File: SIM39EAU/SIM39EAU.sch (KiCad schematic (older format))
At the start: 15 parts, among them IC1 SIM39EA, J1 Conn_01x08, U2 AP7365-W-7

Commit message: Part Numbers Added
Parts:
- BT1: Part (none) -> C238097
- C3: Part (none) -> C396719
- C4: value 1uF -> 4.7uF; Part (none) -> C87998
- D1, D2: Part (none) -> C303800
- R3: Part (none) -> C99198
- R7: Part (none) -> C163436
- R8: Part (none) -> C103426
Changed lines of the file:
@@
 F 2 "Resistor_SMD:R_0603_1608Metric" V 3040 1240 50  0001 C CNN
 F 3 "~" H 3000 1250 50  0001 C CNN
+F 4 "C163436" V 3000 1250 50  0001 C CNN "Part"
 	1    3000 1250
 	0    -1   -1   0
@@
 F 2 "Resistor_SMD:R_0603_1608Metric" V 3240 1540 50  0001 C CNN
 F 3 "~" H 3200 1550 50  0001 C CNN
+F 4 "C103426" H 3200 1550 50  0001 C CNN "Part"
 	1    3200 1550
 	-1   0    0    1
@@
 F 2 "Capacitor_SMD:C_0805_2012Metric" H 1588 1400 50  0001 C CNN
 F 3 "~" H 1550 1550 50  0001 C CNN
+F 4 "C396719" H 1550 1550 50  0001 C CNN "Part"
 	1    1550 1550
 	1    0    0    -1
@@
 F 2 "Resistor_SMD:R_0603_1608Metric" V 1890 1340 50  0001 C CNN
 F 3 "~" H 1850 1350 50  0001 C CNN
+F 4 "C99198" V 1850 1350 50  0001 C CNN "Part"
 	1    1850 1350
 	0    -1   1    0
@@
 P 3450 1550
 F 0 "C4" H 3565 1595 50  0000 L CNN
-F 1 "1uF" H 3565 1505 50  0000 L CNN
+F 1 "4.7uF" H 3565 1505 50  0000 L CNN
 F 2 "Capacitor_SMD:C_0805_2012Metric" H 3488 1400 50  0001 C CNN
 F 3 "~" H 3450 1550 50  0001 C CNN
+F 4 "C87998" H 3450 1550 50  0001 C CNN "Part"
 	1    3450 1550
 	1    0    0    -1
@@
 F 2 "Battery:BatteryHolder_Keystone_3000_1x12mm" V 2700 3410 50  0001 C CNN
 F 3 "~" V 2700 3410 50  0001 C CNN
+F 4 "C238097" H 2700 3350 50  0001 C CNN "Part"
 	1    2700 3350
 	-1   0    0    -1
@@
 F 2 "Diode_SMD:D_SOD-323" H 5100 3100 50  0001 C CNN
 F 3 "https://www.vishay.com/docs/88301/15ke.pdf" H 5050 3300 50  0001 C CNN
+F 4 "C303800" H 5100 3300 50  0001 C CNN "Part"
 	1    5100 3300
 	0    1    1    0
@@
 F 2 "Diode_SMD:D_SOD-323" H 5450 3100 50  0001 C CNN
 F 3 "https://www.vishay.com/docs/88301/15ke.pdf" H 5400 3300 50  0001 C CNN
+F 4 "C303800" H 5450 3300 50  0001 C CNN "Part"
 	1    5450 3300
 	0    1    1    0

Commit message: LED Update
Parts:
- removed R7: 68K, Resistor_SMD:R_0603_1608Metric, symbol Device:R_US
- removed R8: 22K, Resistor_SMD:R_0603_1608Metric, symbol Device:R_US
- removed U2: AP7365-W-7, Package_TO_SOT_SMD:SOT-23-5, symbol Regulator_Linear:AP2127K-ADJ
- added D3: LED, LED_SMD:LED_0603_1608Metric, symbol Device:LED
- added JP1: SolderJumper_2_Bridged, Jumper:SolderJumper-2_P1.3mm_Bridged_RoundedPad1.0x1.5mm, symbol Jumper:SolderJumper_2_Bridged
- added R1: 680E, Resistor_SMD:R_0603_1608Metric, symbol Device:R_US
- added U1: AP2127K-3.3, Package_TO_SOT_SMD:SOT-23-5, symbol Regulator_Linear:AP2127K-3.3
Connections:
- net 3V3: now also JP1.1 (A), U1.5 (VOUT)
- net EN: now also U1.3 (EN)
- net GND: now also D3.1 (K), U1.2 (GND)
- net VIN: now also U1.1 (VIN)
- new net: JP1.2 (B), R1.2
- new net: D3.2 (A), R1.1
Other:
- moved on the sheet: C3, C4
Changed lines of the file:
@@
 Comment4 ""
 $EndDescr
-Text GLabel 3600 1100 2    50   Input ~ 0
+Text GLabel 3550 1250 2    50   Input ~ 0
 3V3
 Wire Wire Line
-	1550 1400 1550 1350
-Wire Wire Line
-	1550 1700 1550 1850
+	1550 1650 1550 1350
+Wire Wire Line
+	1550 1950 1550 2200
 $Comp
 L power:GND #PWR0103
 U 1 1 5DFA7870
-P 2450 1950
-F 0 "#PWR0103" H 2450 1700 50  0001 C CNN
-F 1 "GND" H 2455 1777 50  0000 C CNN
-F 2 "" H 2450 1950 50  0001 C CNN
-F 3 "" H 2450 1950 50  0001 C CNN
-	1    2450 1950
-	1    0    0    -1
-$EndComp
-$Comp
-L Regulator_Linear:AP2127K-ADJ U2
-U 1 1 5E2BA0AD
-P 2450 1350
-F 0 "U2" H 2450 1690 50  0000 C CNN
-F 1 "AP7365-W-7" H 2450 1600 50  0000 C CNN
-F 2 "Package_TO_SOT_SMD:SOT-23-5" H 2450 1675 50  0001 C CNN
-F 3 "https://www.diodes.com/assets/Datasheets/AP2127.pdf" H 2450 1450 50  0001 C CNN
-	1    2450 1350
-	1    0    0    -1
-$EndComp
-$Comp
-L Device:R_US R7
-U 1 1 5E34715F
-P 3000 1250
-F 0 "R7" V 3068 1296 50  0000 L CNN
-F 1 "68K" V 3068 1205 50  0000 R CNN
-F 2 "Resistor_SMD:R_0603_1608Metric" V 3040 1240 50  0001 C CNN
-F 3 "~" H 3000 1250 50  0001 C CNN
-F 4 "C163436" V 3000 1250 50  0001 C CNN "Part"
-	1    3000 1250
-	0    -1   -1   0
-$EndComp
-$Comp
-L Device:R_US R8
-U 1 1 5E35753D
-P 3200 1550
-F 0 "R8" H 3300 1500 50  0000 L CNN
-F 1 "22K" H 3400 1600 50  0000 R CNN
-F 2 "Resistor_SMD:R_0603_1608Metric" V 3240 1540 50  0001 C CNN
-F 3 "~" H 3200 1550 50  0001 C CNN
-F 4 "C103426" H 3200 1550 50  0001 C CNN "Part"
-	1    3200 1550
-	-1   0    0    1
-$EndComp
-Wire Wire Line
-	3200 1350 2750 1350
-Wire Wire Line
-	3150 1250 3200 1250
-Wire Wire Line
-	3200 1400 3200 1350
+P 2450 2300
+F 0 "#PWR0103" H 2450 2050 50  0001 C CNN
+F 1 "GND" H 2455 2127 50  0000 C CNN
+F 2 "" H 2450 2300 50  0001 C CNN
+F 3 "" H 2450 2300 50  0001 C CNN
+	1    2450 2300
+	1    0    0    -1
+$EndComp
 Text GLabel 4500 1300 0    50   Input ~ 0
 TX
@@
 FIX
 Wire Wire Line
-	1550 1850 2450 1850
-Wire Wire Line
-	3200 1700 3200 1850
-Wire Wire Line
-	3200 1350 3200 1250
-Connection ~ 3200 1350
-Wire Wire Line
-	2750 1250 2800 1250
-Wire Wire Line
-	2800 1250 2800 1100
-Connection ~ 2800 1250
-Wire Wire Line
-	2800 1250 2850 1250
-Wire Wire Line
-	2800 1100 3450 1100
+	1550 2200 2450 2200
 $Comp
 L Device:C C3
 U 1 1 5DCB3070
-P 1550 1550
-F 0 "C3" H 1665 1595 50  0000 L CNN
-F 1 "1uF" H 1665 1505 50  0000 L CNN
-F 2 "Capacitor_SMD:C_0805_2012Metric" H 1588 1400 50  0001 C CNN
-F 3 "~" H 1550 1550 50  0001 C CNN
-F 4 "C396719" H 1550 1550 50  0001 C CNN "Part"
-	1    1550 1550
-	1    0    0    -1
-$EndComp
-Wire Wire Line
-	3450 1400 3450 1100
-Connection ~ 3450 1100
-Wire Wire Line
-	3450 1100 3600 1100
-Wire Wire Line
-	3450 1700 3450 1850
-Wire Wire Line
-	3450 1850 3200 1850
-Connection ~ 3200 1850
+P 1550 1800
+F 0 "C3" H 1665 1845 50  0000 L CNN
+F 1 "1uF" H 1665 1755 50  0000 L CNN
+F 2 "Capacitor_SMD:C_0805_2012Metric" H 1588 1650 50  0001 C CNN
+F 3 "~" H 1550 1800 50  0001 C CNN
+F 4 "C396719" H 1550 1800 50  0001 C CNN "Part"
+	1    1550 1800
+	1    0    0    -1
+$EndComp
+Wire Wire Line
+	2975 1950 2975 2200
 Text GLabel 1300 1250 0    50   Input ~ 0
 VIN
@@
 L Device:C C4
 U 1 1 5DB8E885
-P 3450 1550
-F 0 "C4" H 3565 1595 50  0000 L CNN
-F 1 "4.7uF" H 3565 1505 50  0000 L CNN
-F 2 "Capacitor_SMD:C_0805_2012Metric" H 3488 1400 50  0001 C CNN
-F 3 "~" H 3450 1550 50  0001 C CNN
-F 4 "C87998" H 3450 1550 50  0001 C CNN "Part"
-	1    3450 1550
+P 2975 1800
+F 0 "C4" H 3090 1845 50  0000 L CNN
+F 1 "4.7uF" H 3090 1755 50  0000 L CNN
+F 2 "Capacitor_SMD:C_0805_2012Metric" H 3013 1650 50  0001 C CNN
+F 3 "~" H 2975 1800 50  0001 C CNN
+F 4 "C87998" H 2975 1800 50  0001 C CNN "Part"
+	1    2975 1800
 	1    0    0    -1
 $EndComp
@@
 	1    0    0    -1
 $EndComp
-Wire Wire Line
-	2450 1650 2450 1850
-Connection ~ 2450 1850
-Wire Wire Line
-	2450 1850 3200 1850
-Wire Wire Line
-	2450 1850 2450 1950
+Connection ~ 2450 2200
+Wire Wire Line
+	2450 2200 2450 2300
 Wire Wire Line
 	4650 1500 4500 1500
@@
 Wire Wire Line
 	5100 3450 5100 3650
+Wire Wire Line
+	2450 2200 2975 2200
+Wire Wire Line
+	2750 1250 2975 1250
+$Comp
+L Regulator_Linear:AP2127K-3.3 U1
+U 1 1 5DFE50D8
+P 2450 1350
+F 0 "U1" H 2450 1690 50  0000 C CNN
+F 1 "AP2127K-3.3" H 2450 1600 50  0000 C CNN
+F 2 "Package_TO_SOT_SMD:SOT-23-5" H 2450 1675 50  0001 C CNN
+F 3 "https://www.diodes.com/assets/Datasheets/AP2127.pdf" H 2450 1450 50  0001 C CNN
+	1    2450 1350
+	1    0    0    -1
+$EndComp
+Wire Wire Line
+	2975 1650 2975 1250
+Wire Wire Line
+	2450 1650 2450 2200
+Connection ~ 2975 1250
+Connection ~ 2975 2200
+Wire Wire Line
+	2975 1250 3400 1250
+$Comp
+L Jumper:SolderJumper_2_Bridged JP1
+U 1 1 5DFFCA44
+P 3400 1425
+F 0 "JP1" V 3400 1493 50  0000 L CNN
+F 1 "SolderJumper_2_Bridged" V 3445 1493 50  0001 L CNN
+F 2 "Jumper:SolderJumper-2_P1.3mm_Bridged_RoundedPad1.0x1.5mm" H 3400 1425 50  0001 C CNN
+F 3 "~" H 3400 1425 50  0001 C CNN
+	1    3400 1425
+	0    1    1    0
+$EndComp
+$Comp
+L Device:LED D3
+U 1 1 5DFFF072
+P 3400 2050
+F 0 "D3" V 3438 1932 50  0000 R CNN
+F 1 "LED" V 3348 1932 50  0000 R CNN
+F 2 "LED_SMD:LED_0603_1608Metric" H 3400 2050 50  0001 C CNN
+F 3 "~" H 3400 2050 50  0001 C CNN
+F 4 "C193191" V 3400 2050 50  0001 C CNN "Part"
+	1    3400 2050
+	0    -1   -1   0
+$EndComp
+$Comp
+L Device:R_US R1
+U 1 1 5E000844
+P 3400 1750
+F 0 "R1" H 3450 1700 50  0000 L CNN
+F 1 "680E" H 3650 1800 50  0000 R CNN
+F 2 "Resistor_SMD:R_0603_1608Metric" V 3440 1740 50  0001 C CNN
+F 3 "~" H 3400 1750 50  0001 C CNN
+F 4 "C269441" V 3400 1750 50  0001 C CNN "Part"
+	1    3400 1750
+	1    0    0    1
+$EndComp
+Wire Wire Line
+	2975 2200 3400 2200
+Wire Wire Line
+	3400 1600 3400 1575
+Wire Wire Line
+	3400 1275 3400 1250
+Connection ~ 3400 1250
+Wire Wire Line
+	3400 1250 3550 1250
 $EndSCHEMATC

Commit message: Schematic PDF and 3D Renders added
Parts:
- IC1: symbol SIM39EA:SIM39EA -> SIM39EAU-rescue:SIM39EA-SIM39EA
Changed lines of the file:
@@
 	4650 1600 4500 1600
 $Comp
-L SIM39EA:SIM39EA IC1
+L SIM39EAU-rescue:SIM39EA-SIM39EA IC1
 U 1 1 5DC20384
 P 3200 2750

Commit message: SIM39EA Revision 2
Battery connector changed and silkscreens rearranged
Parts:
- BT1: footprint Battery:BatteryHolder_Keystone_3000_1x12mm -> SirBoardLibrary:S8411-45R_1; Part C238097 -> C70381
- C3: value 1uF -> 10uF; Part C396719 -> C95841
- C4: value 4.7uF -> 10uF; Part C87998 -> C95841
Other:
- moved on the sheet: C3, C4
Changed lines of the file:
@@
 Sheet 1 1
 Title "SIM39EA Based GPS Module "
-Date "2019-10-31"
-Rev "1"
+Date "2020-05-13"
+Rev "2"
 Comp "SirBoard"
 Comment1 "SIM39EA is based on the MT3339 Chipset"
@@
 3V3
 Wire Wire Line
-	1550 1650 1550 1350
-Wire Wire Line
-	1550 1950 1550 2200
+	1550 1575 1550 1350
+Wire Wire Line
+	1550 1875 1550 2200
 $Comp
 L power:GND #PWR0103
@@
 L Device:C C3
 U 1 1 5DCB3070
-P 1550 1800
-F 0 "C3" H 1665 1845 50  0000 L CNN
-F 1 "1uF" H 1665 1755 50  0000 L CNN
-F 2 "Capacitor_SMD:C_0805_2012Metric" H 1588 1650 50  0001 C CNN
-F 3 "~" H 1550 1800 50  0001 C CNN
-F 4 "C396719" H 1550 1800 50  0001 C CNN "Part"
-	1    1550 1800
-	1    0    0    -1
-$EndComp
-Wire Wire Line
-	2975 1950 2975 2200
+P 1550 1725
+F 0 "C3" H 1665 1770 50  0000 L CNN
+F 1 "10uF" H 1665 1680 50  0000 L CNN
+F 2 "Capacitor_SMD:C_0805_2012Metric" H 1588 1575 50  0001 C CNN
+F 3 "~" H 1550 1725 50  0001 C CNN
+F 4 "C95841" H 1550 1725 50  0001 C CNN "Part"
+	1    1550 1725
+	1    0    0    -1
+$EndComp
+Wire Wire Line
+	2975 1850 2975 2200
 Text GLabel 1300 1250 0    50   Input ~ 0
 VIN
@@
 L Device:C C4
 U 1 1 5DB8E885
-P 2975 1800
-F 0 "C4" H 3090 1845 50  0000 L CNN
-F 1 "4.7uF" H 3090 1755 50  0000 L CNN
-F 2 "Capacitor_SMD:C_0805_2012Metric" H 3013 1650 50  0001 C CNN
-F 3 "~" H 2975 1800 50  0001 C CNN
-F 4 "C87998" H 2975 1800 50  0001 C CNN "Part"
-	1    2975 1800
+P 2975 1700
+F 0 "C4" H 3090 1745 50  0000 L CNN
+F 1 "10uF" H 3090 1655 50  0000 L CNN
+F 2 "Capacitor_SMD:C_0805_2012Metric" H 3013 1550 50  0001 C CNN
+F 3 "~" H 2975 1700 50  0001 C CNN
+F 4 "C95841" H 2975 1700 50  0001 C CNN "Part"
+	1    2975 1700
 	1    0    0    -1
 $EndComp
@@
 Connection ~ 4750 3050
 Wire Wire Line
-	3200 2950 2500 2950
-Wire Wire Line
-	2500 2950 2500 3650
-Wire Wire Line
-	2500 3650 2700 3650
+	3200 2950 2275 2950
+Wire Wire Line
+	2275 2950 2275 3650
+Wire Wire Line
+	2275 3650 2700 3650
 Connection ~ 3900 3650
 Text GLabel 3050 2750 0    50   Input ~ 0
@@
 F 0 "BT1" H 2818 3445 50  0000 L CNN
 F 1 "CR1220" H 2818 3355 50  0000 L CNN
-F 2 "Battery:BatteryHolder_Keystone_3000_1x12mm" V 2700 3410 50  0001 C CNN
+F 2 "SirBoardLibrary:S8411-45R_1" V 2700 3410 50  0001 C CNN
 F 3 "~" V 2700 3410 50  0001 C CNN
-F 4 "C238097" H 2700 3350 50  0001 C CNN "Part"
+F 4 "C70381" H 2700 3350 50  0001 C CNN "Part"
 	1    2700 3350
 	-1   0    0    -1
@@
 $EndComp
 Wire Wire Line
-	2975 1650 2975 1250
+	2975 1550 2975 1250
 Wire Wire Line
 	2450 1650 2450 2200

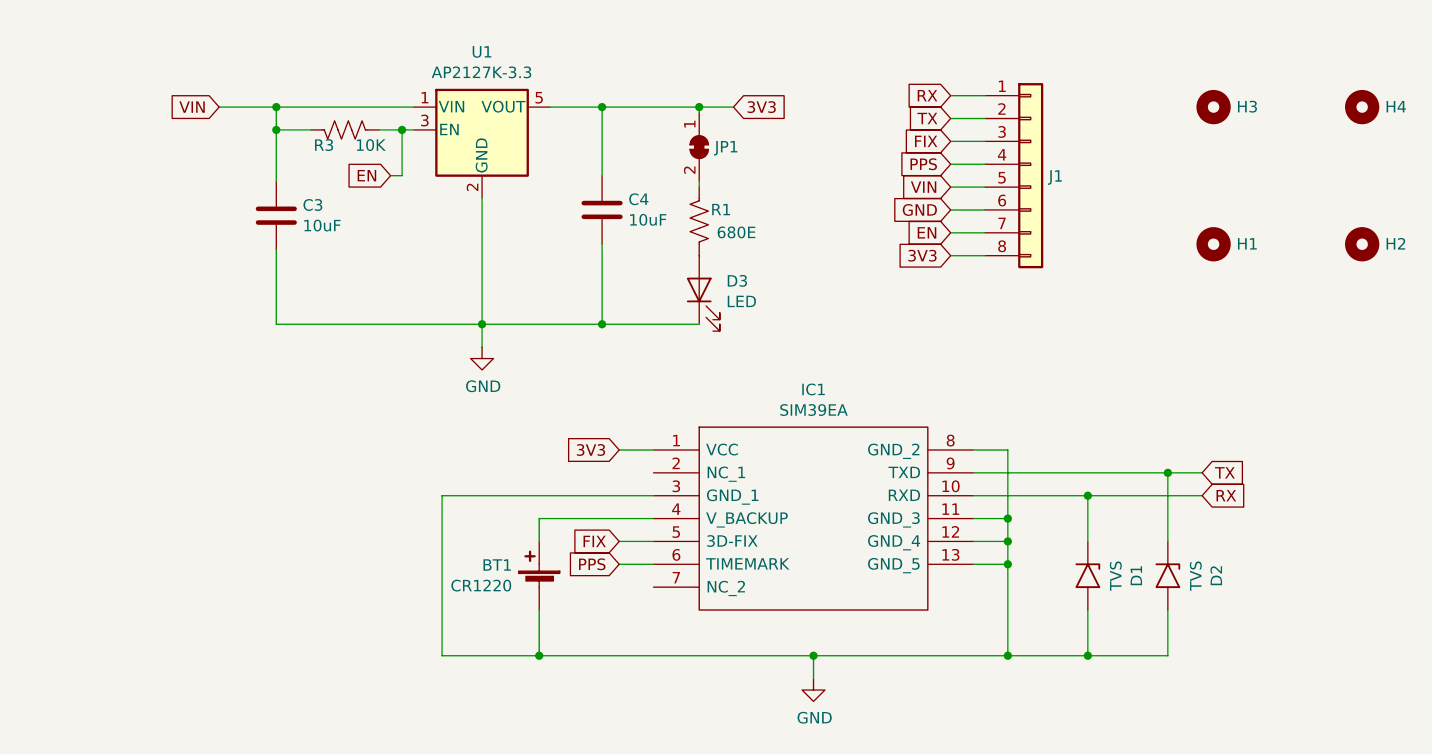
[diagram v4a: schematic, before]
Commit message: SIM39EA Revision 2
Battery Connected
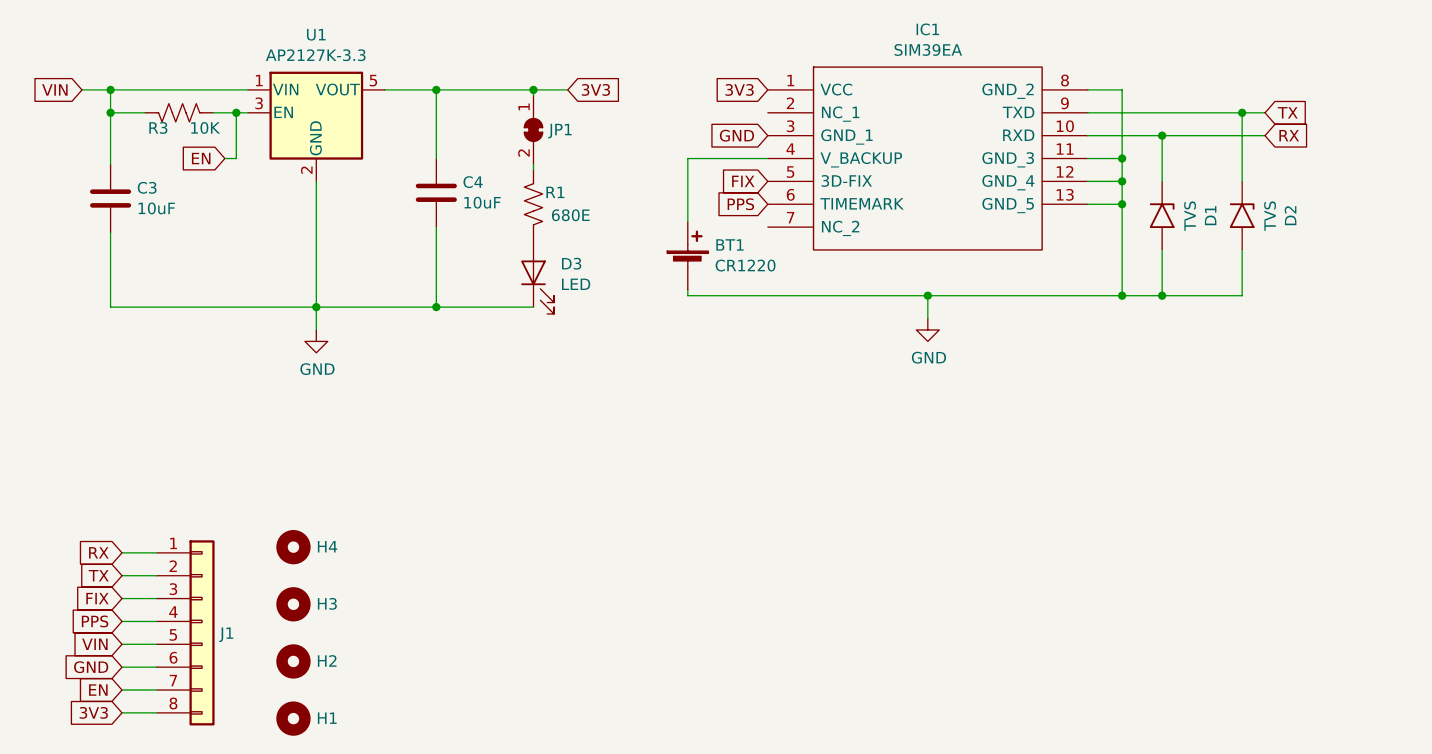
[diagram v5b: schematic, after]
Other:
- moved on the sheet: BT1, C3, C4, D1, D2, D3, H1, H2, H3, H4, IC1, J1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
